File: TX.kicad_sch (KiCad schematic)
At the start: 6 parts, among them J5 LABEL, J6 LABEL, Q2 MJD44H11T4G, Q3 MJD45H11T4G

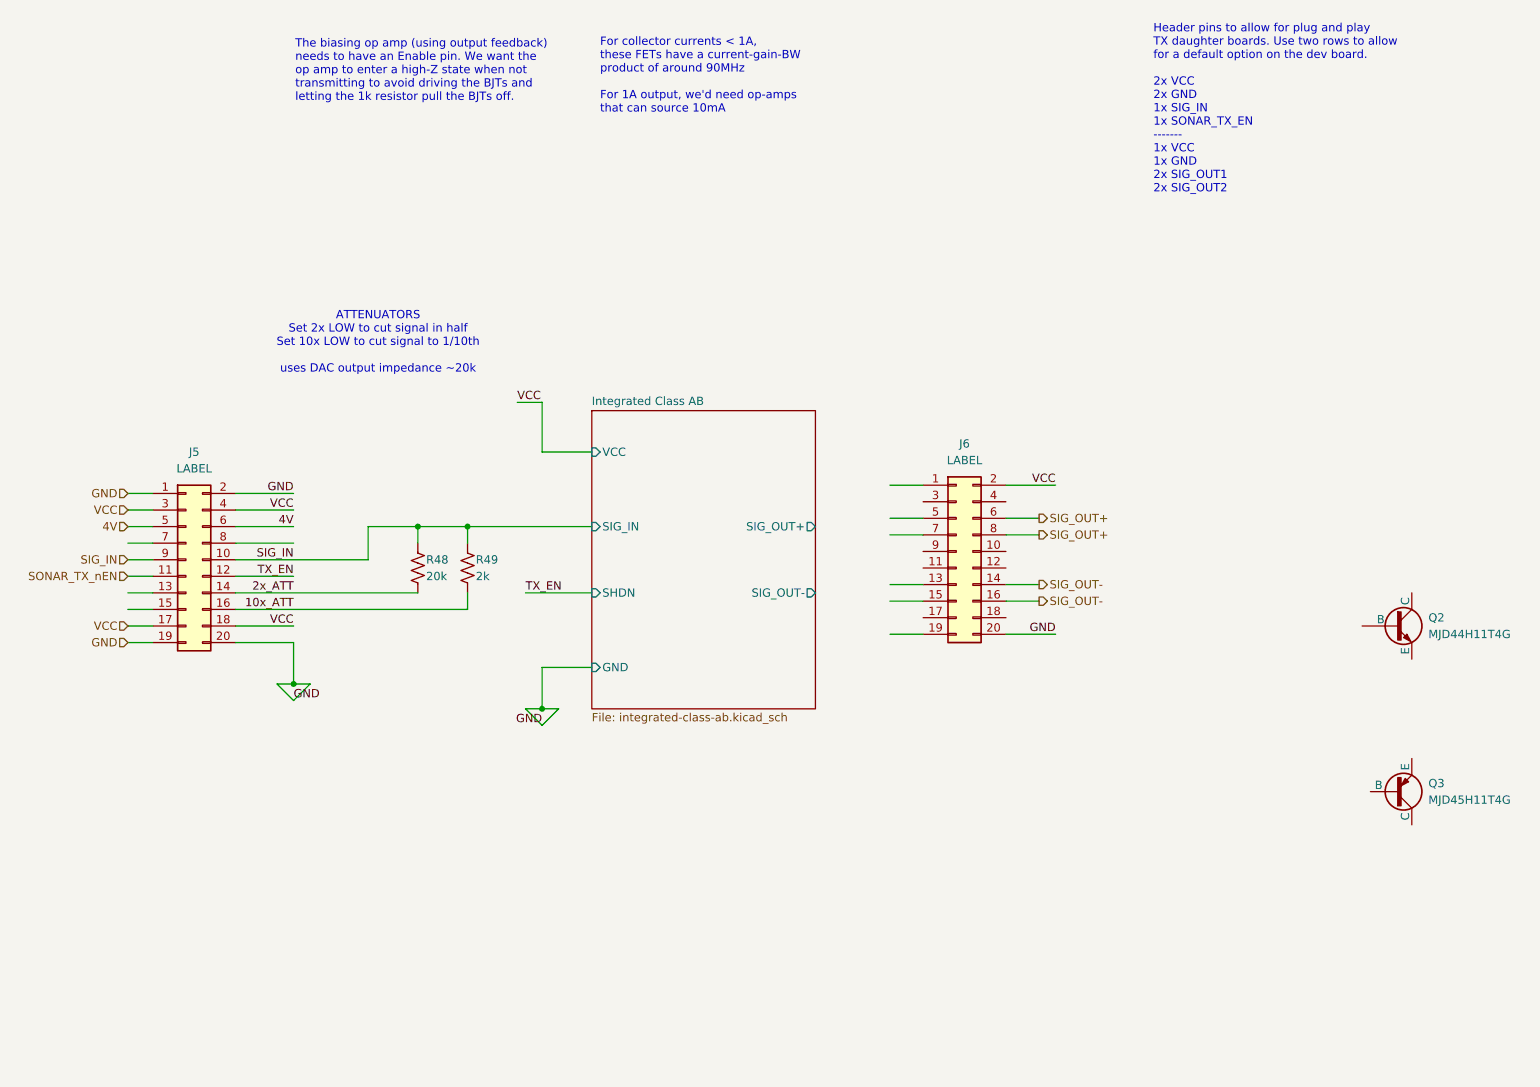
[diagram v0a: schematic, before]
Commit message: Added current sense and shutdown/bias current pin control to LT1794 line driver
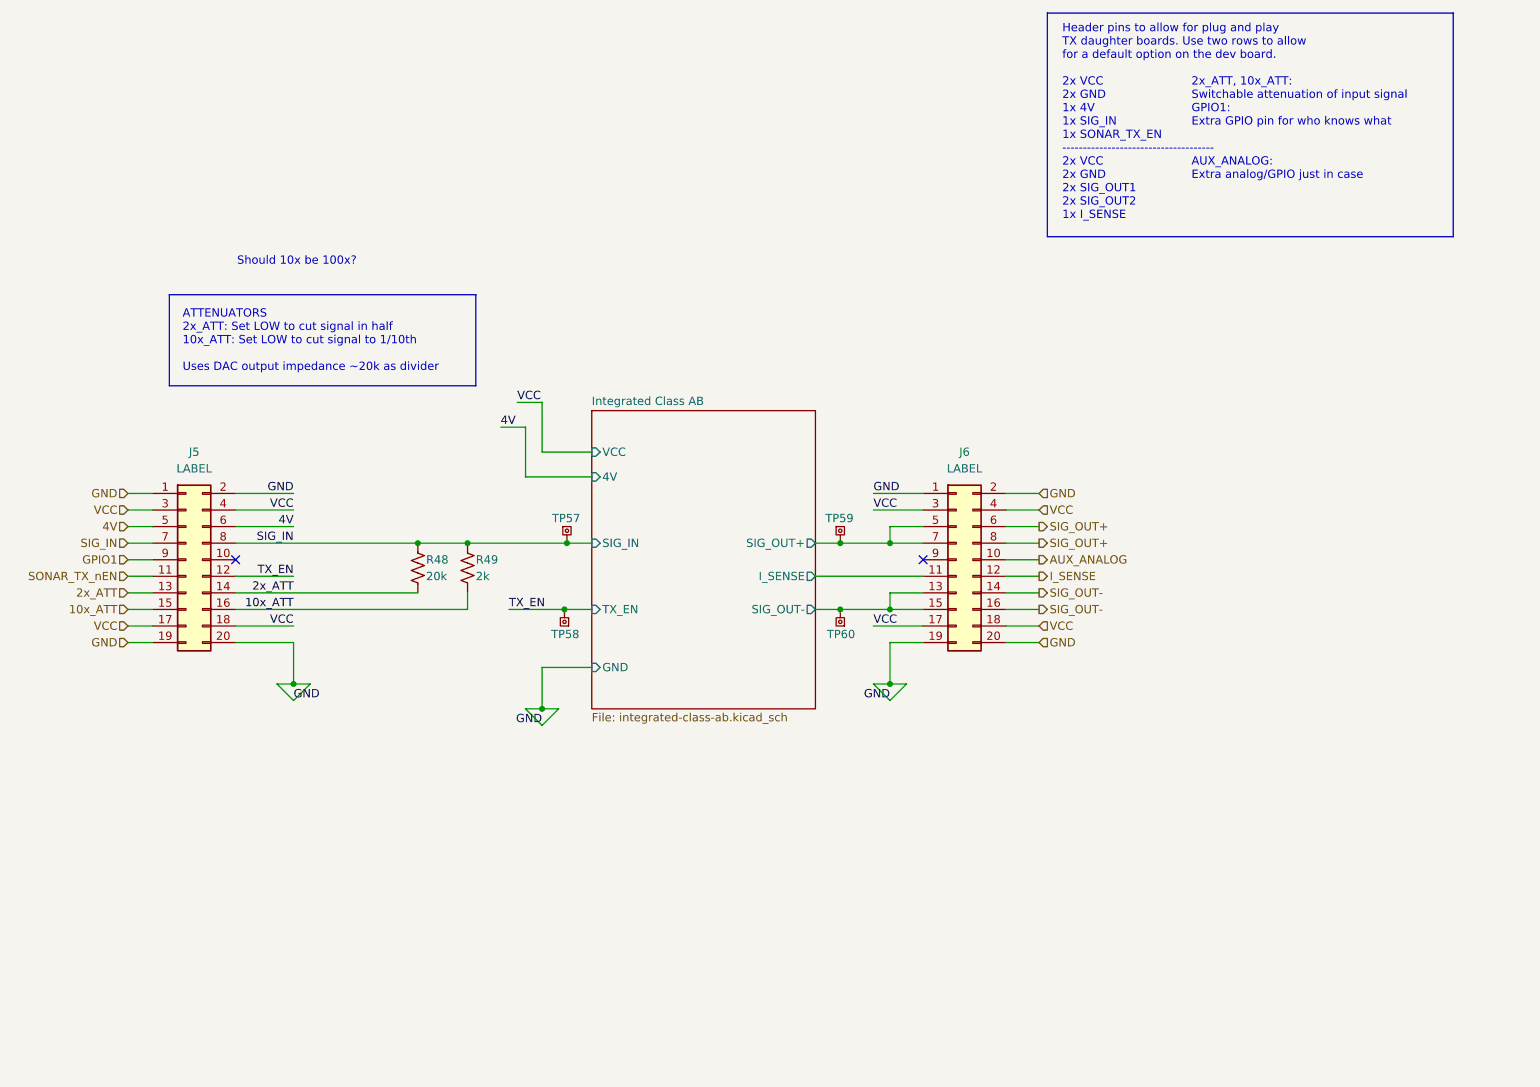
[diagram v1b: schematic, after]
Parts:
- removed Q2: MJD44H11T4G, BR_SOT:TO-252-2_L6.5-W6.1-P4.58-LS10.0-TL, symbol BR_Transistors:BJT_N_MJD44H11T4G
- removed Q3: MJD45H11T4G, BR_SOT:TO-252-2_L6.5-W6.1-P4.58-LS10.0-TL, symbol BR_Transistors:BJT_P_MJD45H11T4G
- added TP57: TX_SIG_IN, BR_Virtual_Parts:TP_SQUARE_TH_1mm, symbol BR_Virtual_Parts:TP_SQUARE_TH_1mm
- added TP58: TX_EN, BR_Virtual_Parts:TP_SQUARE_TH_1mm, symbol BR_Virtual_Parts:TP_SQUARE_TH_1mm
- added TP59: TX_OUT+, BR_Virtual_Parts:TP_SQUARE_TH_1mm, symbol BR_Virtual_Parts:TP_SQUARE_TH_1mm
- added TP60: TX_OUT-, BR_Virtual_Parts:TP_SQUARE_TH_1mm, symbol BR_Virtual_Parts:TP_SQUARE_TH_1mm
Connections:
- net 10x_ATT: now also J5.15 (Pin_15)
- net 2x_ATT: now also J5.13 (Pin_13)
- net GND: now also J6.1 (Pin_1), J6.19 (Pin_19), J6.2 (Pin_2)
- net Integrated Class AB/SIG_OUT+: now also J6.5 (Pin_5), J6.7 (Pin_7), TP59.1
- net Integrated Class AB/SIG_OUT-: now also J6.13 (Pin_13), J6.15 (Pin_15), TP60.1
- net SIG_IN: now also J5.7 (Pin_7), J5.8 (Pin_8), TP57.1; no longer J5.10 (Pin_10), J5.9 (Pin_9)
- net TX_EN: now also TP58.1
- net VCC: now also J6.17 (Pin_17), J6.18 (Pin_18), J6.3 (Pin_3), J6.4 (Pin_4); no longer J6.2 (Pin_2)
- net AUX_ANALOG: now reaches J6.10 (Pin_10)
- net Integrated Class AB/I_SENSE: now reaches J6.11 (Pin_11)
- net I_SENSE: now reaches J6.12 (Pin_12)
- new net GPIO1: J5.9 (Pin_9)
- no-connect marks 0 -> 2
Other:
- sheet Integrated Class AB ports: added 4V, I_SENSE, TX_EN; removed SHDN
- note added: "2x_ATT, 10x_ATT: Switchable attenuation of input signal GPIO1: Extra GPIO pin for who knows what AUX_ANALOG: Extra analog/GPIO just in case"
- note added: "ATTENUATORS 2x_ATT: Set LOW to cut signal in half 10x_ATT: Set LOW to cut signal to 1/10th Uses DAC output impedance ~20k as divider"
- note added: "Header pins to allow for plug and play TX daughter boards. Use two rows to allow for a default option on the dev board. 2x VCC 2x GND 1x 4V 1x SIG_IN 1x SONAR_TX_EN ------------------------------------- 2x VCC 2x GND 2x SIG_OUT1 2x SIG_OUT2 1x I_SENSE"
- note added: "Should 10x be 100x?"
- note removed: "ATTENUATORS Set 2x LOW to cut signal in half Set 10x LOW to cut signal to 1/10th uses DAC output impedance ~20k"
- note removed: "For collector currents < 1A, these FETs have a current-gain-BW product of around 90MHz For 1A output, we'd need op-amps that can source 10mA"
- note removed: "Header pins to allow for plug and play TX daughter boards. Use two rows to allow for a default option on the dev board. 2x VCC 2x GND 1x SIG_IN 1x SONAR_TX_EN ------- 1x VCC 1x GND 2x SIG_OUT1 2x SIG_OUT2"
- note removed: "The biasing op amp (using output feedback) needs to have an Enable pin. We want the op amp to enter a high-Z state when not transmitting to avoid driving the BJTs and letting the 1k resistor pull the BJTs off."
- moved on the sheet: J6

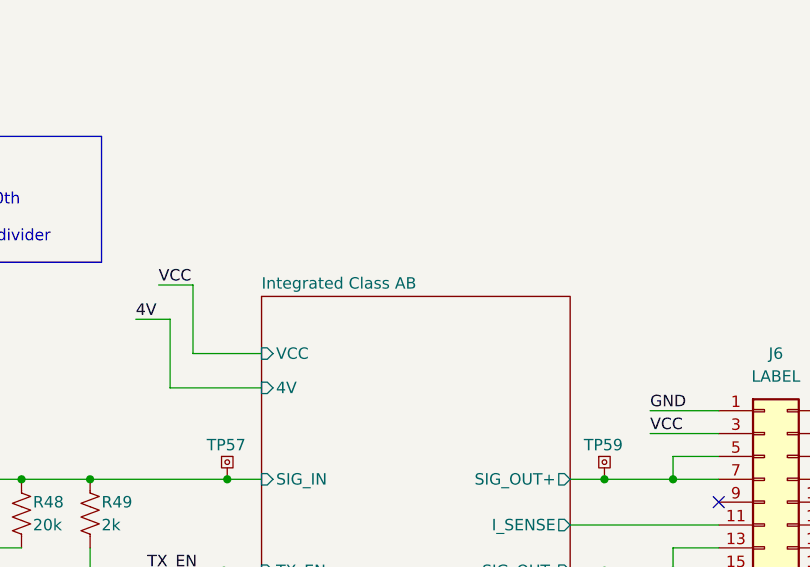
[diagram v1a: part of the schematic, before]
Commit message: changed name of LT1794 hierarchical sheet
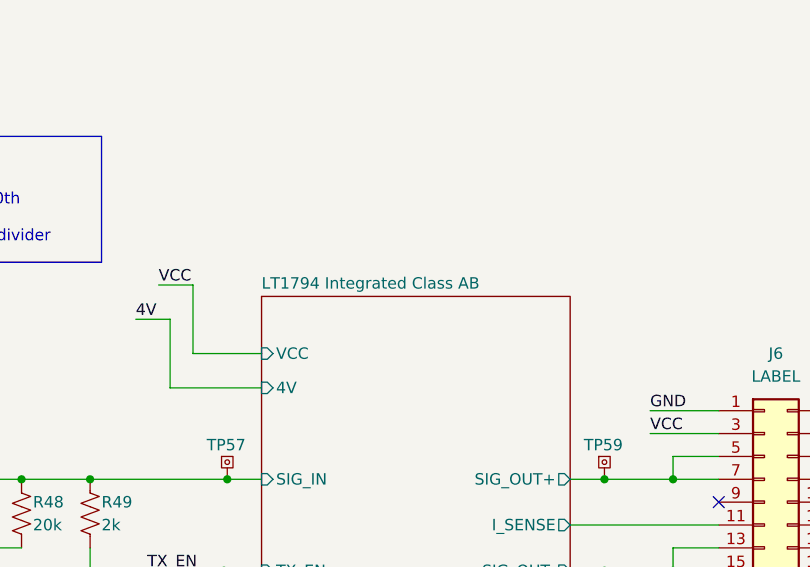
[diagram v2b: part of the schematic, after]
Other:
- sheet Integrated Class AB renamed LT1794 Integrated Class AB
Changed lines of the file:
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@@
 			(color 255 12 21 0.1900)
 		)
-		(property "Sheetname" "Integrated Class AB"
+		(property "Sheetname" "LT1794 Integrated Class AB"
 			(at 146.05 72.9484 0)
 			(effects

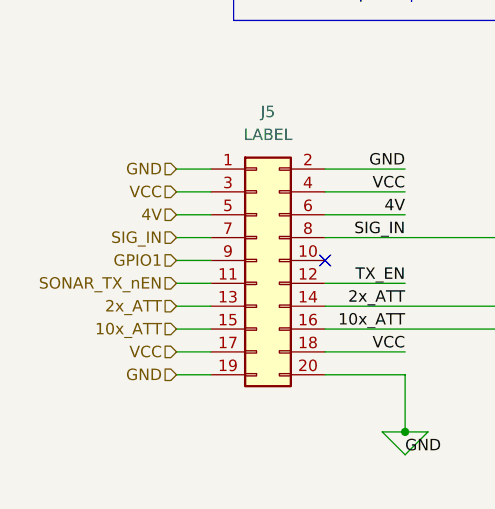
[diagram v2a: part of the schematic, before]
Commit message: Tentatively finished with TX schematic
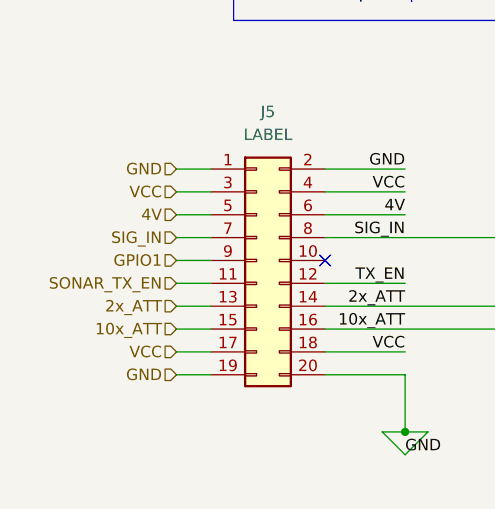
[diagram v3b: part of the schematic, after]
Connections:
- net SONAR_TX_nEN renamed SONAR_TX_EN
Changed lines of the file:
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@@
 		)
 	)
-	(hierarchical_label "SONAR_TX_nEN"
+	(hierarchical_label "SONAR_TX_EN"
 		(shape input)
 		(at 74.93 99.06 180)

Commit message: various updates + digital drive sheet
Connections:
- net 10x_ATT: no longer J5.16 (Pin_16), R49.2
- net 2x_ATT: no longer J5.14 (Pin_14), R48.2
- net 4V: no longer J5.6 (Pin_6)
- net GND: no longer J5.2 (Pin_2), J5.20 (Pin_20), J6.1 (Pin_1), J6.19 (Pin_19)
- net SIG_IN: no longer J5.8 (Pin_8), R48.1, R49.1, TP57.1
- net VCC: no longer J5.18 (Pin_18), J5.4 (Pin_4), J6.17 (Pin_17), J6.3 (Pin_3)
- net LT1794 Integrated Class AB/I_SENSE renamed I_SENSE_AB
- net LT1794 Integrated Class AB/SIG_OUT+ renamed SIG_OUT+_AB
- net LT1794 Integrated Class AB/SIG_OUT- renamed SIG_OUT-_AB
- net TX_EN renamed TX_EN_AB
- new net 10x_ATT_AB: J5.16 (Pin_16), R49.2
- new net 2x_ATT_AB: J5.14 (Pin_14), R48.2
- new net 4V_AB: J5.6 (Pin_6)
- new net GND_AB: J5.2 (Pin_2), J5.20 (Pin_20), J6.1 (Pin_1), J6.19 (Pin_19)
- new net SIG_IN_AB: J5.8 (Pin_8), R48.1, R49.1, TP57.1
- new net VCC_AB: J5.18 (Pin_18), J5.4 (Pin_4), J6.17 (Pin_17), J6.3 (Pin_3)
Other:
- added sheet Digital Drive (digital_drive.kicad_sch)
- moved on the sheet: J6

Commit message: rewiring STM32H563
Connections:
- net 4V renamed 5V
- net 4V_AB renamed 5V_AB
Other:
- sheet LT1794 Integrated Class AB ports: added 5V; removed 4V
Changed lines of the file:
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@@
 		)
 	)
-	(label "4V_AB"
+	(label "5V_AB"
 		(at 102.87 91.44 180)
 		(effects
@@
 		)
 	)
-	(label "4V_AB"
+	(label "5V_AB"
 		(at 132.08 83.82 0)
 		(effects
@@
 		)
 	)
-	(hierarchical_label "4V"
+	(hierarchical_label "5V"
 		(shape input)
 		(at 74.93 91.44 180)
@@
 			)
 		)
-		(pin "4V" input
-			(at 146.05 83.82 180)
-			(effects
-				(font
-					(size 1.27 1.27)
-				)
-				(justify left)
-			)
-		)
 		(pin "I_SENSE" output
 			(at 180.34 99.06 0)
@@
 			(effects
 				(font
+					(size 1.27 1.27)
+				)
+				(justify left)
+			)
+		)
+		(pin "5V" input
+			(at 146.05 83.82 180)
+			(effects
+				(font

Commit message: added rj45 and h-bridge + stm pinout spreadsheet
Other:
- sheet Digital Drive ports: added PWM_A, PWM_B, SIG_OUT+, SIG_OUT-, VCC; removed none
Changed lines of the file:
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@@
+			)
+		)
+		(pin "PWM_A" input
+			(at 101.6 148.59 180)
+			(effects
+				(font
+					(size 1.27 1.27)
+				)
+				(justify left)
+			)
+		)
+		(pin "PWM_B" input
+			(at 101.6 151.13 180)
+			(effects
+				(font
+					(size 1.27 1.27)
+				)
+				(justify left)
+			)
+		)
+		(pin "SIG_OUT+" output
+			(at 127 149.86 0)
+			(effects
+				(font
+					(size 1.27 1.27)
+				)
+				(justify right)
+			)
+		)
+		(pin "SIG_OUT-" output
+			(at 127 152.4 0)
+			(effects
+				(font
+					(size 1.27 1.27)
+				)
+				(justify right)
+			)
+		)
+		(pin "VCC" input
+			(at 101.6 144.78 180)
+			(effects
+				(font
+					(size 1.27 1.27)
+				)
+				(justify left)
 			)
 		)

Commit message: added to STM pinout + boost fixes
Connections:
- net 10x_ATT renamed 10X_ATT
- net 10x_ATT_AB renamed 10X_ATT_AB
- net 2x_ATT renamed 2X_ATT
- net 2x_ATT_AB renamed 2X_ATT_AB
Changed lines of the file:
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@@
+	(wire
+		(pts
+			(xy 92.71 154.94) (xy 101.6 154.94)
+		)
+		(stroke
+			(width 0)
+			(type default)
+		)
+	)
 	(wire
 		(pts
@@
 	(wire
 		(pts
+			(xy 127 154.94) (xy 137.16 154.94)
+		)
+		(stroke
+			(width 0)
+			(type default)
+		)
+	)
+	(wire
+		(pts
 			(xy 195.58 101.6) (xy 195.58 104.14)
 		)
@@
 	(wire
 		(pts
+			(xy 92.71 151.13) (xy 101.6 151.13)
+		)
+		(stroke
+			(width 0)
+			(type default)
+		)
+	)
+	(wire
+		(pts
 			(xy 127 93.98) (xy 142.24 93.98)
 		)
@@
 	(wire
 		(pts
+			(xy 92.71 144.78) (xy 101.6 144.78)
+		)
+		(stroke
+			(width 0)
+			(type default)
+		)
+	)
+	(wire
+		(pts
 			(xy 208.28 88.9) (xy 200.66 88.9)
 		)
@@
 		(pts
 			(xy 138.43 113.03) (xy 138.43 119.38)
+		)
+		(stroke
+			(width 0)
+			(type default)
+		)
+	)
+	(wire
+		(pts
+			(xy 127 151.13) (xy 137.16 151.13)
 		)
 		(stroke
@@
 		)
 	)
-	(label "10x_ATT_AB"
+	(label "10X_ATT_AB"
 		(at 102.87 104.14 180)
 		(effects
@@
 		)
 	)
-	(label "2x_ATT_AB"
+	(label "2X_ATT_AB"
 		(at 102.87 101.6 180)
 		(effects
@@
 		)
 	)
-	(hierarchical_label "10x_ATT"
+	(hierarchical_label "SIG_OUT-"
+		(shape output)
+		(at 137.16 154.94 0)
+		(effects
+			(font
+				(size 1.27 1.27)
+			)
+			(justify left)
+		)
+	)
+	(hierarchical_label "10X_ATT"
 		(shape input)
 		(at 74.93 104.14 180)
@@
 		)
 	)
+	(hierarchical_label "VCC"
+		(shape input)
+		(at 92.71 144.78 180)
+		(effects
+			(font
+				(size 1.27 1.27)
+			)
+			(justify right)
+		)
+	)
 	(hierarchical_label "GND"
 		(shape input)
@@
 		)
 	)
+	(hierarchical_label "SIG_OUT+"
+		(shape output)
+		(at 137.16 151.13 0)
+		(effects
+			(font
+				(size 1.27 1.27)
+			)
+			(justify left)
+		)
+	)
+	(hierarchical_label "PWM_B"
+		(shape input)
+		(at 92.71 154.94 180)
+		(effects
+			(font
+				(size 1.27 1.27)
+			)
+			(justify right)
+		)
+	)
 	(hierarchical_label "VCC"
 		(shape input)
@@
 		)
 	)
-	(hierarchical_label "2x_ATT"
+	(hierarchical_label "2X_ATT"
 		(shape input)
 		(at 74.93 101.6 180)
+		(effects
+			(font
+				(size 1.27 1.27)
+			)
+			(justify right)
+		)
+	)
+	(hierarchical_label "PWM_A"
+		(shape input)
+		(at 92.71 151.13 180)
 		(effects
 			(font
@@
 	(sheet
 		(at 101.6 139.7)
-		(size 25.4 25.4)
+		(size 25.4 22.86)
 		(exclude_from_sim no)
 		(in_bom yes)
@@
 		)
 		(property "Sheetfile" "digital_drive.kicad_sch"
-			(at 101.6 165.6846 0)
+			(at 101.6 163.1446 0)
 			(effects
 				(font
@@
 		)
 		(pin "PWM_A" input
-			(at 101.6 148.59 180)
+			(at 101.6 151.13 180)
 			(effects
 				(font
@@
 		)
 		(pin "PWM_B" input
-			(at 101.6 151.13 180)
+			(at 101.6 154.94 180)
 			(effects
 				(font
@@
 		)
 		(pin "SIG_OUT+" output
-			(at 127 149.86 0)
+			(at 127 151.13 0)
 			(effects
 				(font
@@
 		)
 		(pin "SIG_OUT-" output
-			(at 127 152.4 0)
-			(effects
-				(font
+			(at 127 154.94 0)
+			(effects
+				(font

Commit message: completed feedback from review + reannotated sheets
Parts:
- renumbered J5 to J501, J6 to J502, R48 to R501, R49 to R502, TP58 to TP501, TP57 to TP502, TP59 to TP503, TP60 to TP504
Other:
- sheet Digital Drive ports: added 5V, SD0, SD1; removed none
